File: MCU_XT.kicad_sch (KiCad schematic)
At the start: 31 parts, among them J10 SWD, J11 UART, J12 I2C1, Q16 AO3401A, Q17 2N7002W, U12 STM32F030C8Tx

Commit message: ported more changes from previous version
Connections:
- net +3V3: no longer C112.1, C113.1, C114.1, C115.1, C117.1, C118.1, J10.1 (Pin_1), J11.1 (Pin_1), R19.1, R20.1, R33.1, R34.1, R85.2, R86.2, U12.1 (VDD), U12.24 (VDD), U12.48 (VDD), U12.9 (VDDA)
- net PB7: now reaches U12.43 (PB7)
- new net +3V3MCU: C112.1, C113.1, C114.1, C115.1, C117.1, C118.1, J10.1 (Pin_1), J11.1 (Pin_1), R19.1, R20.1, R33.1, R34.1, R85.2, R86.2, U12.1 (VDD), U12.24 (VDD), U12.48 (VDD), U12.9 (VDDA)
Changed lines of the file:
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@@
 		)
 	)
+	(hierarchical_label "PB7"
+		(shape bidirectional)
+		(at 40.64 91.44 180)
+		(effects
+			(font
+				(size 1.27 1.27)
+			)
+			(justify right)
+		)
+	)
 	(hierarchical_label "SDA1"
 		(shape bidirectional)
@@
 		(on_board yes)
 		(dnp no)
-		(fields_autoplaced yes)
 		(property "Reference" "#PWR0125"
 			(at 81.28 73.66 0)
@@
 			)
 		)
-		(property "Value" "+3V3"
+		(property "Value" "+3V3MCU"
 			(at 81.28 64.77 0)
 			(effects
@@
 					(size 1.27 1.27)
 				)
+				(justify left)
 			)
 		)
@@
 		(on_board yes)
 		(dnp no)
-		(fields_autoplaced yes)
 		(property "Reference" "#PWR0119"
 			(at 30.48 41.91 0)
@@
 			)
 		)
-		(property "Value" "+3V3"
-			(at 30.48 33.02 0)
+		(property "Value" "+3V3MCU"
+			(at 30.226 33.274 0)
 			(effects
 				(font
 					(size 1.27 1.27)
 				)
+				(justify left)
 			)
 		)
@@
 		(on_board yes)
 		(dnp no)
-		(fields_autoplaced yes)
 		(property "Reference" "#PWR0128"
 			(at 111.76 99.06 0)
@@
 			)
 		)
-		(property "Value" "+3V3"
-			(at 111.76 90.17 0)
+		(property "Value" "+3V3MCU"
+			(at 111.76 89.916 0)
 			(effects
 				(font
 					(size 1.27 1.27)
 				)
+				(justify left)
 			)
 		)
@@
 		(on_board yes)
 		(dnp no)
-		(fields_autoplaced yes)
 		(property "Reference" "#PWR0124"
 			(at 55.88 35.56 0)
@@
 			)
 		)
-		(property "Value" "+3V3"
-			(at 55.88 26.67 0)
+		(property "Value" "+3V3MCU"
+			(at 55.88 27.686 0)
 			(effects
 				(font
 					(size 1.27 1.27)
 				)
+				(justify left)
 			)
 		)
@@
 		(on_board yes)
 		(dnp no)
-		(fields_autoplaced yes)
 		(property "Reference" "#PWR067"
 			(at 91.44 99.06 0)
@@
 			)
 		)
-		(property "Value" "+3V3"
-			(at 91.44 90.17 0)
+		(property "Value" "+3V3MCU"
+			(at 91.186 89.916 0)
 			(effects
 				(font
 					(size 1.27 1.27)
 				)
+				(justify left)
 			)
 		)
@@
 		(on_board yes)
 		(dnp no)
-		(fields_autoplaced yes)
 		(property "Reference" "#PWR01"
 			(at 97.79 63.5 0)
@@
 			)
 		)
-		(property "Value" "+3V3"
-			(at 97.79 54.61 0)
+		(property "Value" "+3V3MCU"
+			(at 97.79 54.356 0)
 			(effects
 				(font
 					(size 1.27 1.27)
 				)
+				(justify left)
 			)
 		)
@@
 		(on_board yes)
 		(dnp no)
-		(fields_autoplaced yes)
 		(property "Reference" "#PWR068"
 			(at 19.05 69.85 0)
@@
 			)
 		)
-		(property "Value" "+3V3"
+		(property "Value" "+3V3MCU"
 			(at 19.05 60.96 0)
 			(effects
@@
 					(size 1.27 1.27)
 				)
+				(justify left)
 			)
 		)
@@
 		(on_board yes)
 		(dnp no)
-		(fields_autoplaced yes)
 		(property "Reference" "#PWR0123"
 			(at 101.6 33.02 0)
@@
 			)
 		)
-		(property "Value" "+3V3"
+		(property "Value" "+3V3MCU"
 			(at 101.6 24.13 0)
 			(effects
@@
 					(size 1.27 1.27)
 				)
+				(justify left)
 			)
 		)

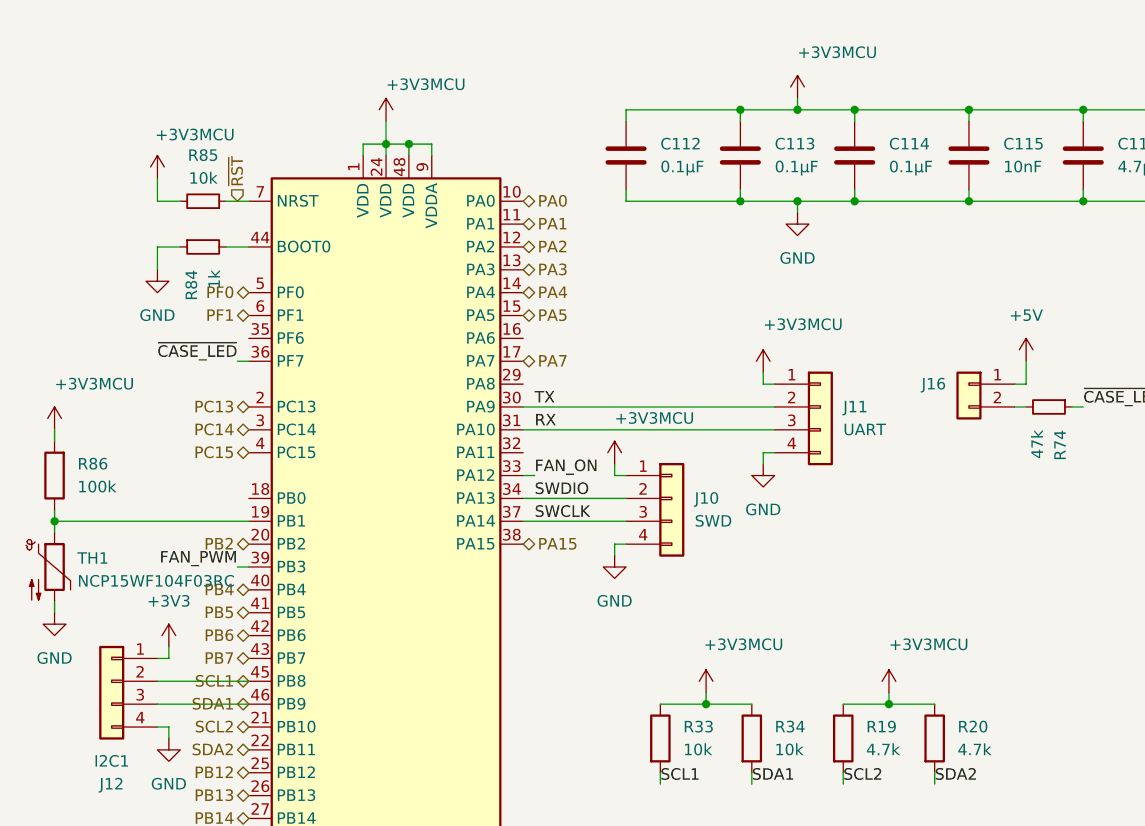
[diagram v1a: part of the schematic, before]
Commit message: added more missing functionality to start psu
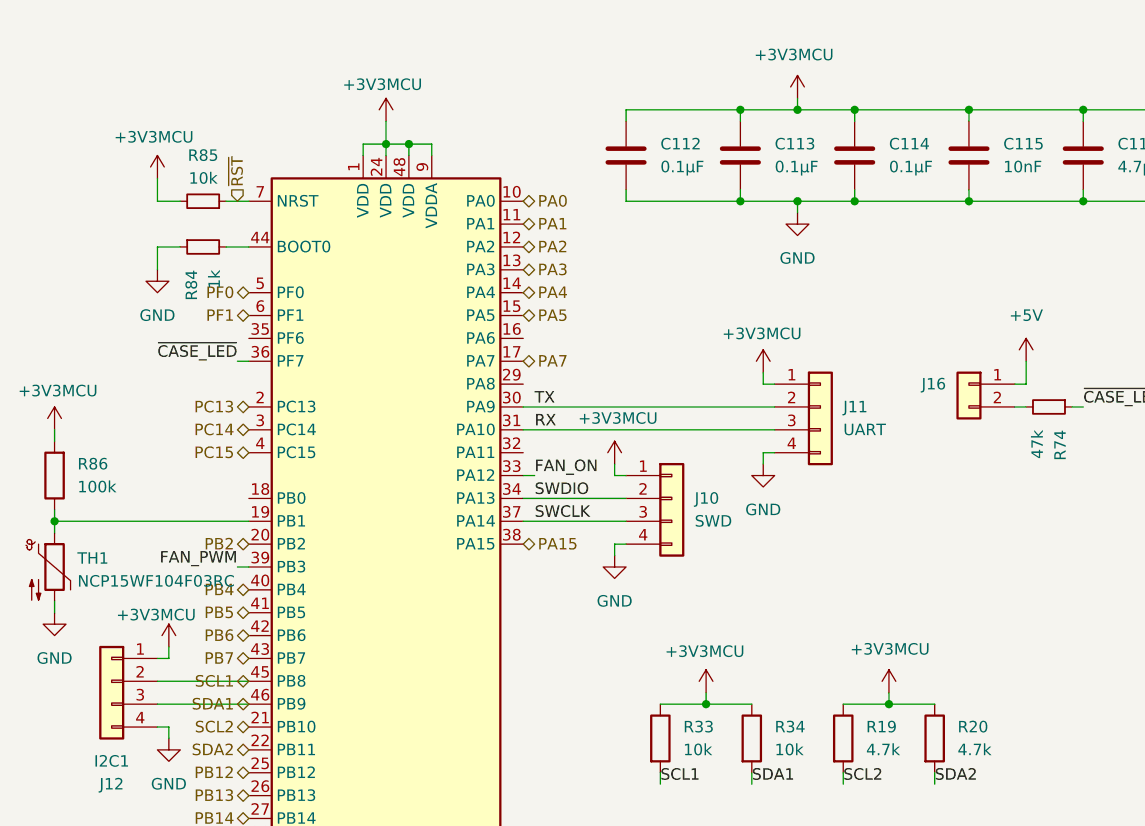
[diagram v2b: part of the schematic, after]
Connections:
- net +3V3 is gone; now on net +3V3MCU: J12.1 (Pin_1)
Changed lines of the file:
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@@
 		)
 		(property "Value" "+3V3MCU"
-			(at 81.28 64.77 0)
+			(at 77.216 64.77 0)
 			(effects
 				(font
@@
 		)
 		(property "Value" "+3V3MCU"
-			(at 30.226 33.274 0)
+			(at 25.654 33.528 0)
 			(effects
 				(font
@@
 		)
 		(property "Value" "+3V3MCU"
-			(at 111.76 89.916 0)
+			(at 107.442 90.424 0)
 			(effects
 				(font
@@
 		)
 		(property "Value" "+3V3MCU"
-			(at 55.88 27.686 0)
+			(at 51.054 27.686 0)
 			(effects
 				(font
@@
 		)
 		(property "Value" "+3V3MCU"
-			(at 91.186 89.916 0)
+			(at 86.868 90.678 0)
 			(effects
 				(font
@@
 		(on_board yes)
 		(dnp no)
-		(fields_autoplaced yes)
 		(property "Reference" "#PWR018"
 			(at 31.75 93.98 0)
@@
 			)
 		)
-		(property "Value" "+3V3"
-			(at 31.75 85.09 0)
+		(property "Value" "+3V3MCU"
+			(at 25.908 86.614 0)
 			(effects
 				(font
 					(size 1.27 1.27)
 				)
+				(justify right)
 			)
 		)
@@
 		)
 		(property "Value" "+3V3MCU"
-			(at 97.79 54.356 0)
+			(at 93.218 55.372 0)
 			(effects
 				(font
@@
 		)
 		(property "Value" "+3V3MCU"
-			(at 19.05 60.96 0)
+			(at 14.986 61.722 0)
 			(effects
 				(font
@@
 		)
 		(property "Value" "+3V3MCU"
-			(at 101.6 24.13 0)
+			(at 96.774 24.384 0)
 			(effects
 				(font
